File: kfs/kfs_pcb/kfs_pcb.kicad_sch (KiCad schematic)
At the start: 75 parts, among them SW0 SWITCH, SW1 SWITCH, SW10 SWITCH, SW11 SWITCH, SW12 SWITCH, SW13 SWITCH, SW14 SWITCH, SW15 SWITCH, SW16 SWITCH, SW17 SWITCH, SW18 SWITCH, SW19 SWITCH, SW2 SWITCH, SW20 SWITCH, SW21 SWITCH, SW22 SWITCH, SW23 SWITCH, SW24 SWITCH, SW25 SWITCH, SW26 SWITCH, SW27 SWITCH, SW28 SWITCH, SW29 SWITCH, SW3 SWITCH, SW30 SWITCH, SW31 SWITCH, SW32 SWITCH, SW33 SWITCH, SW34 SWITCH, SW35 SWITCH, SW36 SWITCH, SW37 SWITCH, SW38 SWITCH, SW39 SWITCH, SW4 SWITCH, SW40 SWITCH, SW41 SWITCH, SW42 SWITCH, SW43 SWITCH, SW44 SWITCH, SW45 SWITCH, SW46 SWITCH, SW47 SWITCH, SW48 SWITCH, SW49 SWITCH, SW5 SWITCH, SW50 SWITCH, SW51 SWITCH, SW52 SWITCH, SW53 SWITCH, SW54 SWITCH, SW55 SWITCH, SW56 SWITCH, SW57 SWITCH, SW58 SWITCH, SW59 SWITCH, SW6 SWITCH, SW60 SWITCH, SW61 SWITCH, SW62 SWITCH, SW63 SWITCH, SW7 SWITCH, SW8 SWITCH, SW9 SWITCH, U0 ARDUINO_PRO_MICRO

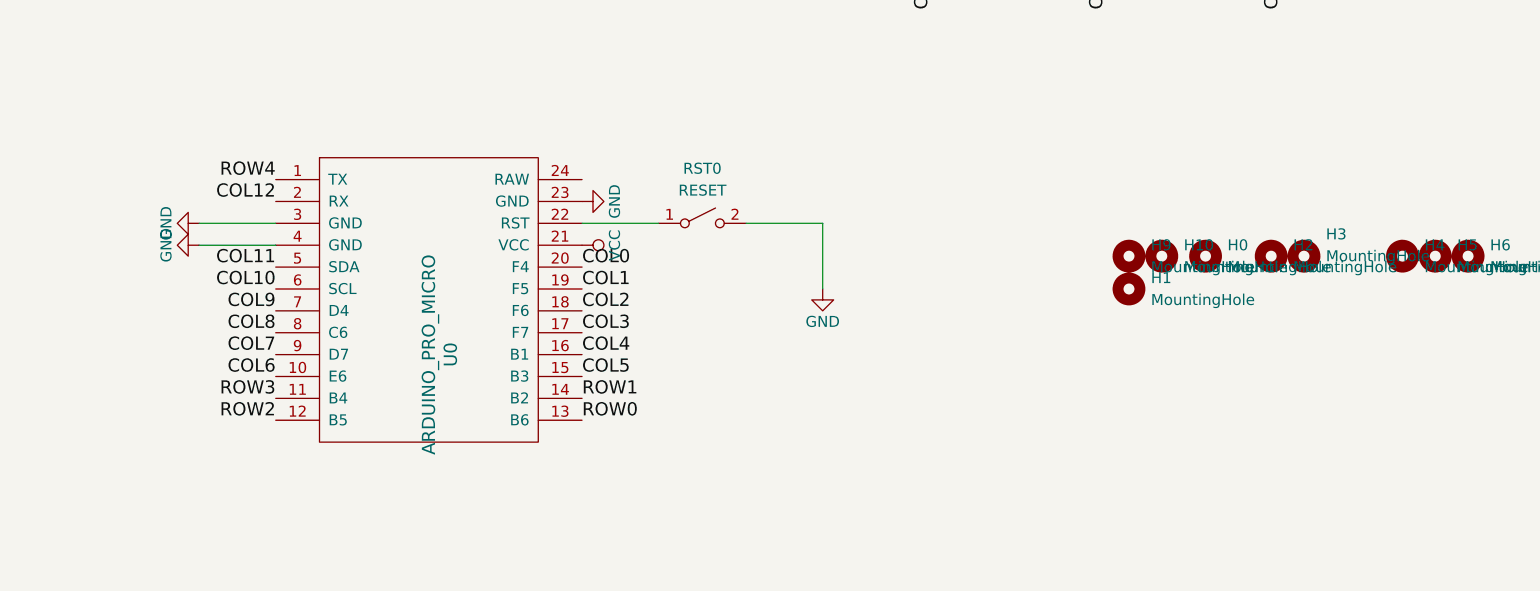
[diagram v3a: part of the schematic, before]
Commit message: Switched kfs to use nice!nano.
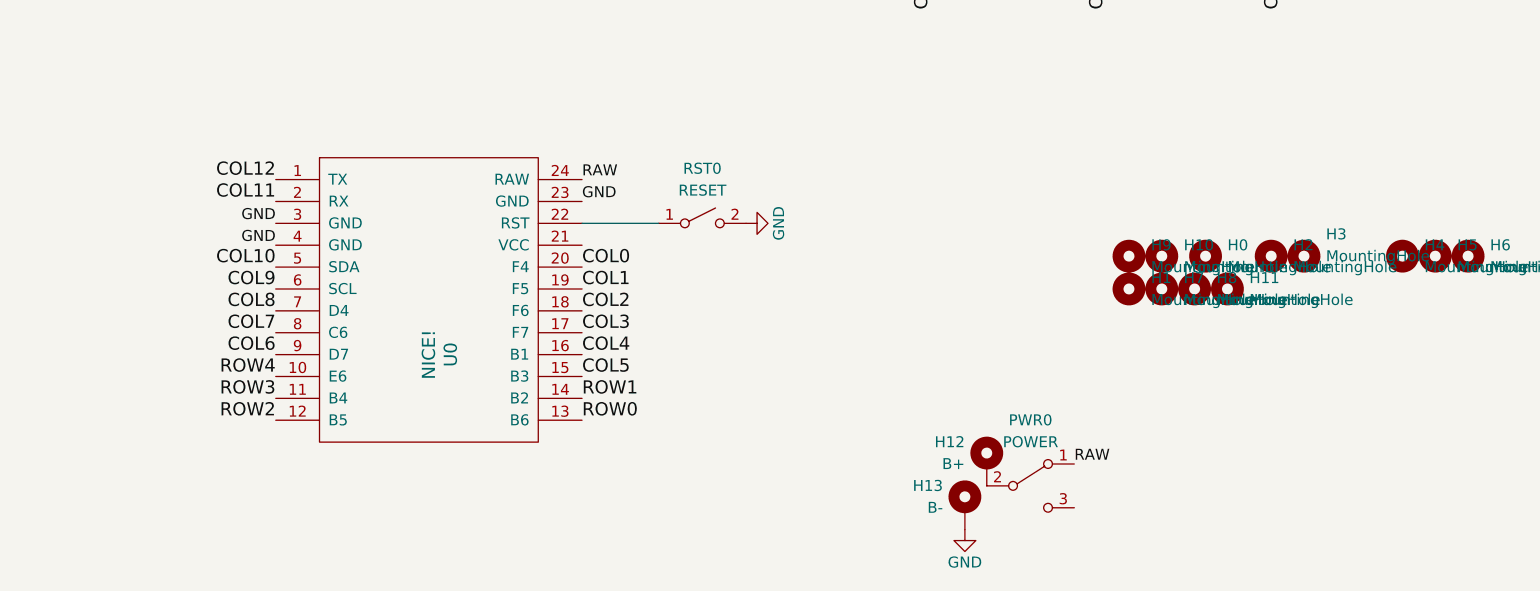
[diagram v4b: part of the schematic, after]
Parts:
- added H11, H7, H8: MountingHole, MountingHole:MountingHole_3.5mm, symbol Mechanical:MountingHole
- added H12: B+, Connector_Pin:Pin_D0.9mm_L10.0mm_W2.4mm_FlatFork, symbol Mechanical:MountingHole_Pad
- added H13: B-, Connector_Pin:Pin_D0.9mm_L10.0mm_W2.4mm_FlatFork, symbol Mechanical:MountingHole_Pad
- added PWR0: POWER, footprints:AYZ0102AGRLC, symbol Switch:SW_SPDT
- U0: value ARDUINO_PRO_MICRO -> NICE!; footprint footprints:ARDUINO_PRO_MICRO -> footprints:nice!nano
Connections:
- net COL10: now also U0.5 (SDA); no longer U0.6 (SCL)
- net COL11: now also U0.2 (RX); no longer U0.5 (SDA)
- net COL12: now also U0.1 (TX); no longer U0.2 (RX)
- net COL6: now also U0.9 (D7); no longer U0.10 (E6)
- net COL7: now also U0.8 (C6); no longer U0.9 (D7)
- net COL8: now also U0.7 (D4); no longer U0.8 (C6)
- net COL9: now also U0.6 (SCL); no longer U0.7 (D4)
- net GND: now also H13.1
- net ROW4: now also U0.10 (E6); no longer U0.1 (TX)
- net RAW: now reaches U0.24 (RAW)
- net RAW: now also PWR0.1 (A)
- net VCC: no longer names the net of U0.21 (VCC)
- new net: H12.1, PWR0.2 (B)

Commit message: Changed the reset and power switches for kfs and jlk.
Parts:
- PWR0: footprint footprints:AYZ0102AGRLC -> footprints:power_switch
- RST0: footprint footprints:reset_button_1 -> footprints:reset_button_2
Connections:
- net GND: now also RST0.1 (A); no longer RST0.2 (B)
- net at U0.22 (RST): now also RST0.2 (B); no longer RST0.1 (A)
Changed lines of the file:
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@@
     )
   )
-  (symbol (lib_id "Switch:SW_SPST") (at 212.09 149.86 0) (unit 1)
-    (in_bom yes) (on_board yes) (dnp no) (fields_autoplaced)
+  (symbol (lib_id "Switch:SW_SPST") (at 212.09 149.86 0) (mirror y) (unit 1)
+    (in_bom yes) (on_board yes) (dnp no)
     (property "Reference" "RST0" (at 212.09 143.51 0)
       (effects (font (size 1.27 1.27)))
@@
       (effects (font (size 1.27 1.27)))
     )
-    (property "Footprint" "footprints:reset_button_1" (at 212.09 149.86 0)
+    (property "Footprint" "footprints:reset_button_2" (at 212.09 149.86 0)
       (effects (font (size 1.27 1.27)) hide)
     )
@@
       (effects (font (size 1.27 1.27)))
     )
-    (property "Footprint" "footprints:AYZ0102AGRLC" (at 250.19 180.34 0)
-      (effects (font (size 1.27 1.27)) hide)
-    )
+    (property "Footprint" "footprints:power_switch" (at 250.19 180.34 0)
+      (effects (font (size 1.27 1.27)) hide)
+    )

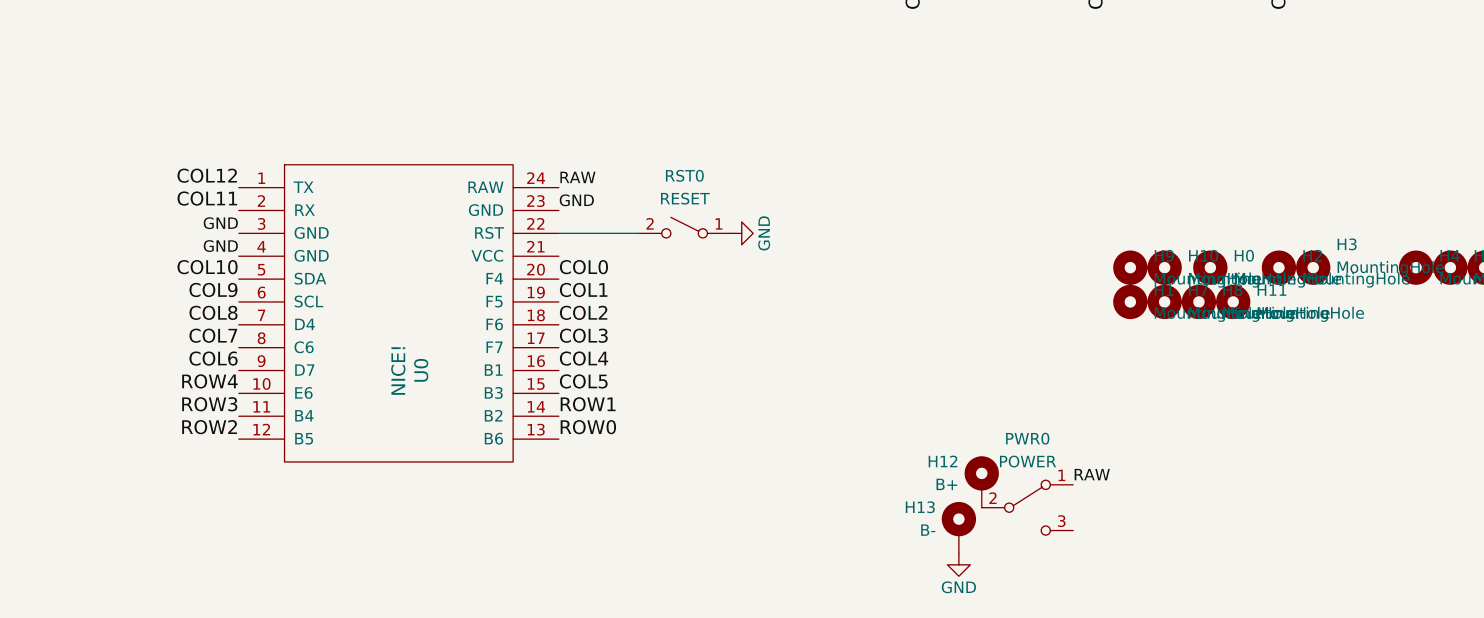
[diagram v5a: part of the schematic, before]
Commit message: Moved mcu to underside of pcb, added battery jack.
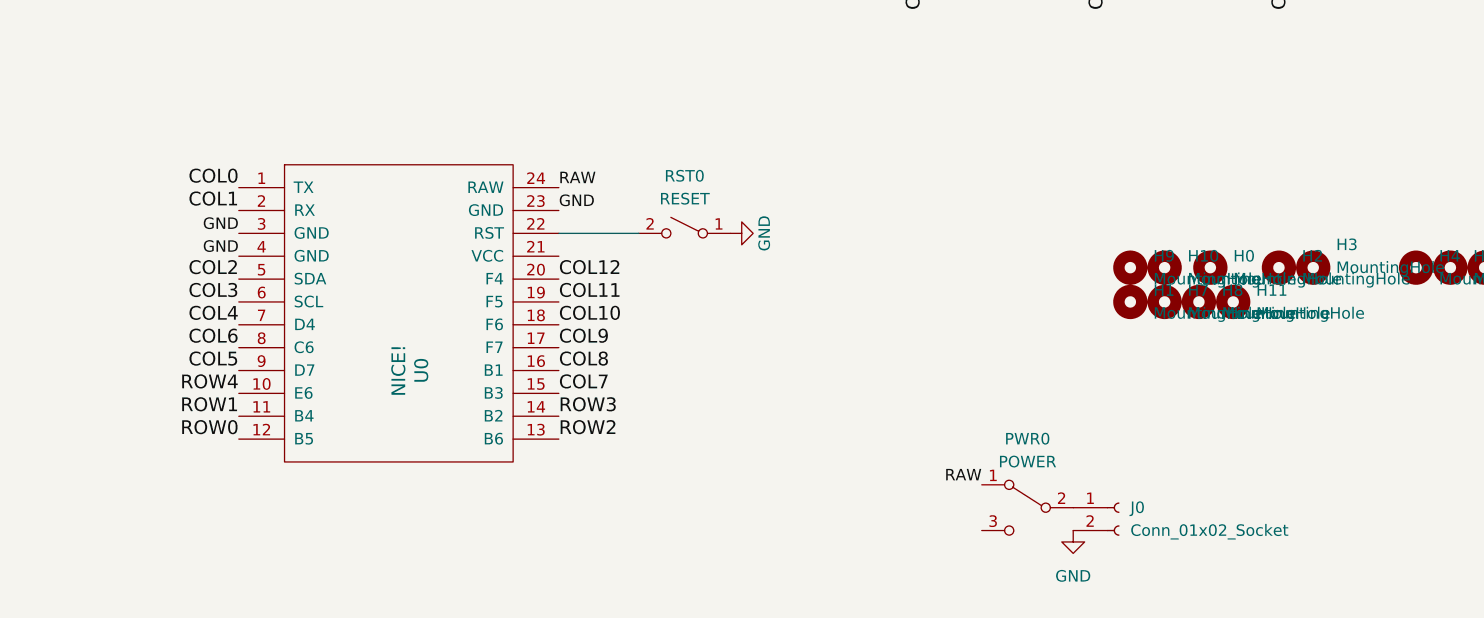
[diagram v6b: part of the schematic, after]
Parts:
- removed H12: B+, Connector_Pin:Pin_D0.9mm_L10.0mm_W2.4mm_FlatFork, symbol Mechanical:MountingHole_Pad
- removed H13: B-, Connector_Pin:Pin_D0.9mm_L10.0mm_W2.4mm_FlatFork, symbol Mechanical:MountingHole_Pad
- added J0: Conn_01x02_Socket, footprints:jst_ph, symbol Connector:Conn_01x02_Socket
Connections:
- net COL0: now also U0.1 (TX); no longer U0.20 (F4)
- net COL1: now also U0.2 (RX); no longer U0.19 (F5)
- net COL10: now also U0.18 (F6); no longer U0.5 (SDA)
- net COL11: now also U0.19 (F5); no longer U0.2 (RX)
- net COL12: now also U0.20 (F4); no longer U0.1 (TX)
- net COL2: now also U0.5 (SDA); no longer U0.18 (F6)
- net COL3: now also U0.6 (SCL); no longer U0.17 (F7)
- net COL4: now also U0.7 (D4); no longer U0.16 (B1)
- net COL5: now also U0.9 (D7); no longer U0.15 (B3)
- net COL6: now also U0.8 (C6); no longer U0.9 (D7)
- net COL7: now also U0.15 (B3); no longer U0.8 (C6)
- net COL8: now also U0.16 (B1); no longer U0.7 (D4)
- net COL9: now also U0.17 (F7); no longer U0.6 (SCL)
- net GND: now also J0.2 (Pin_2)
- net ROW0: now also U0.12 (B5); no longer U0.13 (B6)
- net ROW1: now also U0.11 (B4); no longer U0.14 (B2)
- net ROW2: now also U0.13 (B6); no longer U0.12 (B5)
- net ROW3: now also U0.14 (B2); no longer U0.11 (B4)
- net at PWR0.2 (B): now also J0.1 (Pin_1)

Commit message: Small changes.
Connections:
- net GND: now also J0.1 (Pin_1); no longer J0.2 (Pin_2)
- net at PWR0.2 (B): now also J0.2 (Pin_2); no longer J0.1 (Pin_1)
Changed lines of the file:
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@@
     )
   )
-  (symbol (lib_id "Connector:Conn_01x02_Socket") (at 260.35 180.34 0) (unit 1)
-    (in_bom yes) (on_board yes) (dnp no) (fields_autoplaced)
-    (property "Reference" "J0" (at 261.62 180.34 0)
+  (symbol (lib_id "Connector:Conn_01x02_Socket") (at 260.35 182.88 0) (mirror x) (unit 1)
+    (in_bom yes) (on_board yes) (dnp no)
+    (property "Reference" "J0" (at 261.62 182.88 0)
       (effects (font (size 1.27 1.27)) (justify left))
     )
-    (property "Value" "Conn_01x02_Socket" (at 261.62 182.88 0)
+    (property "Value" "Conn_01x02_Socket" (at 261.62 180.34 0)
       (effects (font (size 1.27 1.27)) (justify left))
     )
-    (property "Footprint" "footprints:jst_ph" (at 260.35 180.34 0)
+    (property "Footprint" "footprints:jst_ph" (at 260.35 182.88 0)
       (effects (font (size 1.27 1.27)) hide)
     )
-    (property "Datasheet" "~" (at 260.35 180.34 0)
+    (property "Datasheet" "~" (at 260.35 182.88 0)
       (effects (font (size 1.27 1.27)) hide)
     )
